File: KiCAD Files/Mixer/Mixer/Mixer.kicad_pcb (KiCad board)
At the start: 4 copper layers, 59 x 30.5 mm, 64 parts, among them IC1 FST3253MTCX, K1 G6K-2F-Y DC3, U1 OPA1678IDGKT, U2 OPA1678IDGKT, U3 OPA1678IDGKT, U4 NC7SZ04P5X, U5 4053, U6 4053

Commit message: update only
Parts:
- removed IQ_Clk: Conn_01x04_Socket, Connector_PinHeader_2.54mm:PinHeader_1x04_P2.54mm_Vertical
- added IQ_Clock_in1: Conn_01x03_Socket, Connector_JST:JST_EH_B3B-EH-A_1x03_P2.50mm_Vertical, F.Cu at (107.0, 82.9)
- added JP1: SolderJumper_3_Open, Jumper:SolderJumper-3_P1.3mm_Open_Pad1.0x1.5mm_NumberLabels, B.Cu at (119.9, 84.2)
- added JP2: SolderJumper_3_Open, Jumper:SolderJumper-3_P1.3mm_Open_Pad1.0x1.5mm_NumberLabels, B.Cu at (134.2, 84.8)
- added R5: 100R, Resistor_SMD:R_0805_2012Metric_Pad1.20x1.40mm_HandSolder, B.Cu at (126.4, 84.8)
- added R8: 100R, Resistor_SMD:R_0805_2012Metric_Pad1.20x1.40mm_HandSolder, B.Cu at (117.0, 75.1)
- added U2: SN74AC74PWR, Private:74AC74-L, B.Cu at (120.2, 71.2)
- renumbered IQ_Balance to IQ_Balance1, I_In_Tx to I_In_Tx1, I_Out_Rx to I_Out_Rx1, Q_In_Tx to Q_In_Tx1, Q_Out_Rx to Q_Out_Rx1, R8 to R10, R9 to R11, R10 to R12, R11 to R13, R12 to R14, R13 to R15, R14 to R16, R15 to R17, R16 to R18, R17 to R19, R18 to R20, R5 to R6, R6 to R7, R7 to R9, RF_In to RF_In1, RF_Out to RF_Out1, Supply to Supply1, Tx to Tx2, TxN to TxN1, U2 to U3, U3 to U4, U4 to U5, U5 to U6, U6 to U7
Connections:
- IC1 pad 14: /Clk_S0 -> /S0
- IC1 pad 2: /Clk_S1 -> /S1
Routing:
- net /S0: track 0.00 -> 21.2 mm
- net /Clk_S0: track 21.2 -> 0.00 mm
- net /S1: track 0.00 -> 15.7 mm
- net /Clk_S1: track 15.7 -> 0.00 mm

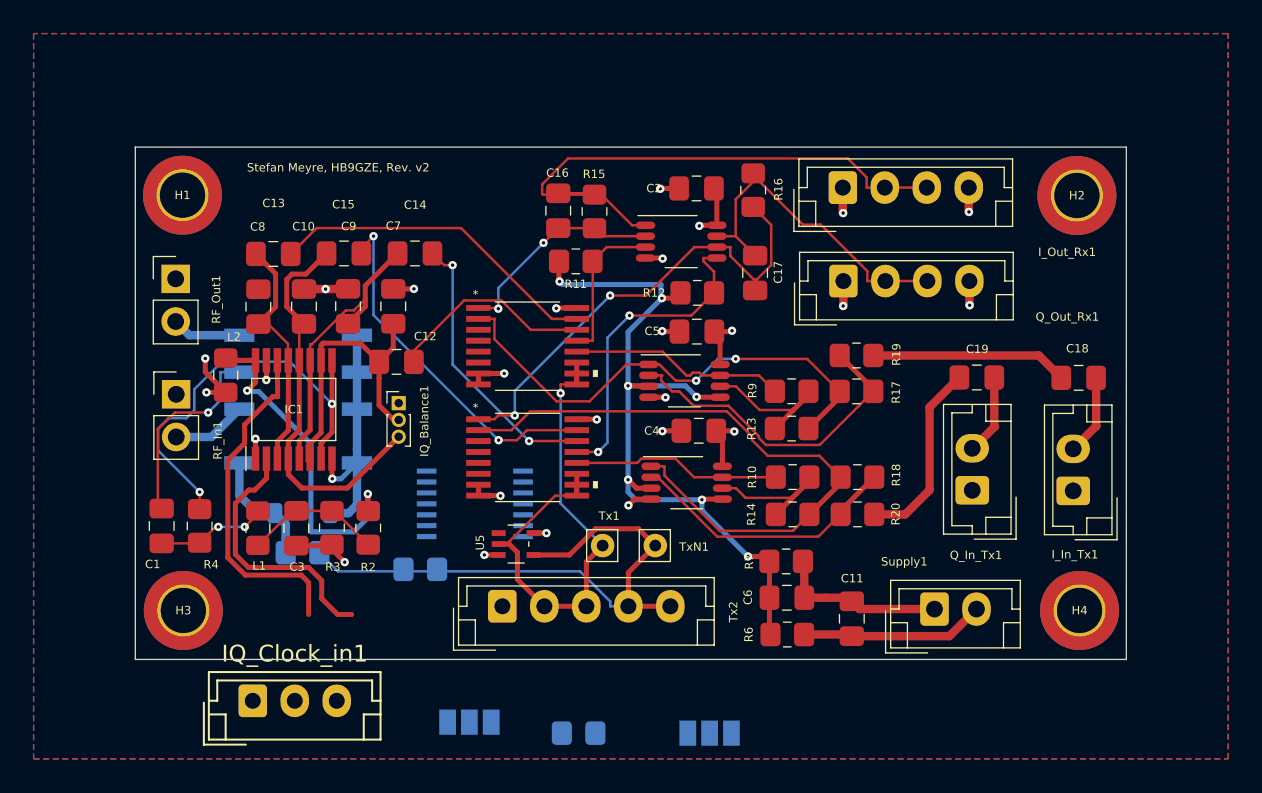
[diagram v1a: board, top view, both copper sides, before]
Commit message: added 74AC74 at mixer board
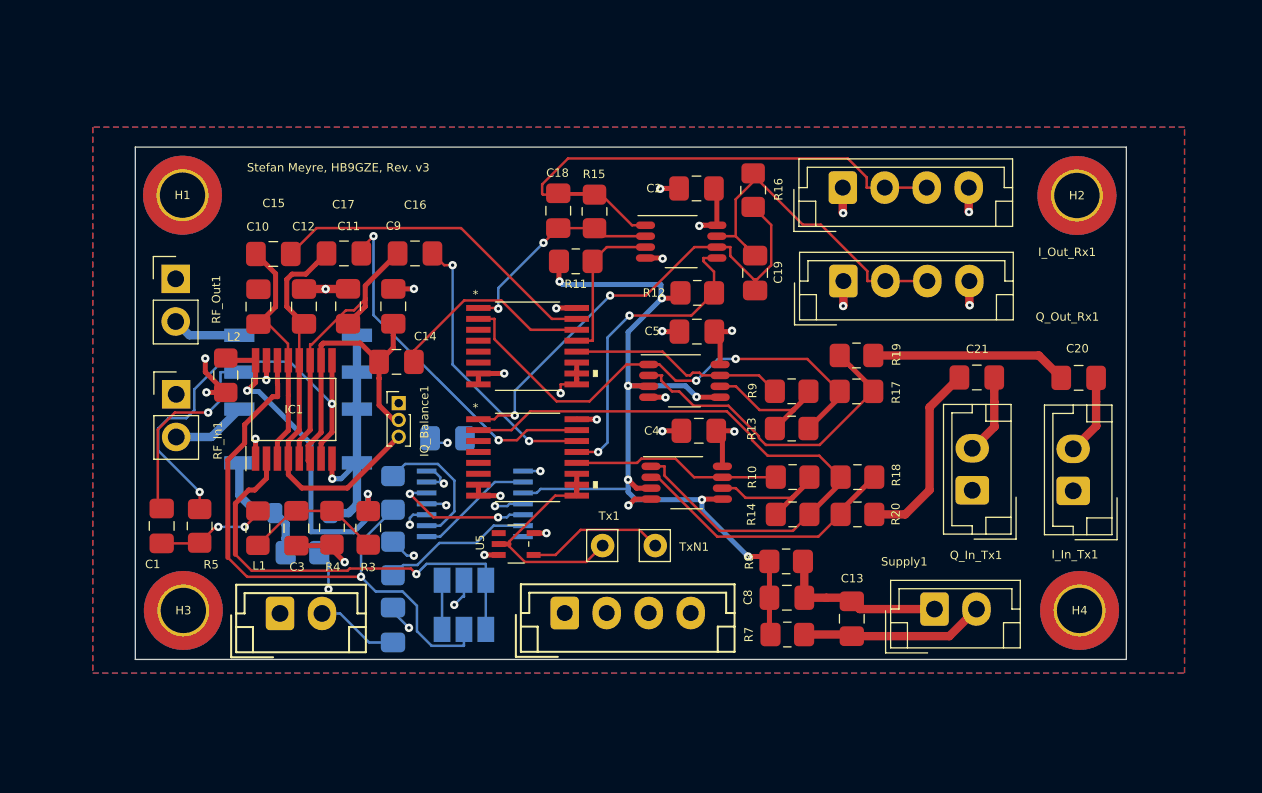
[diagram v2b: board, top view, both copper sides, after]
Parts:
- removed IQ_Clock_in1: Conn_01x03_Socket, Connector_JST:JST_EH_B3B-EH-A_1x03_P2.50mm_Vertical
- removed the R5 at (126.4, 84.8)
- removed the R8 at (117.0, 75.1)
- removed Tx2: Conn_01x05_Socket, Connector_JST:JST_EH_B5B-EH-A_1x05_P2.50mm_Vertical
- added C6: 100nF, Capacitor_SMD:C_0805_2012Metric_Pad1.18x1.45mm_HandSolder, B.Cu at (115.4, 78.4)
- added C7: 10uF, Capacitor_SMD:C_0805_2012Metric_Pad1.18x1.45mm_HandSolder, B.Cu at (118.6, 67.3)
- added J1: Conn_01x02_Socket, Connector_JST:JST_EH_B2B-EH-A_1x02_P2.50mm_Vertical, F.Cu at (108.7, 77.7)
- added J2: Conn_01x04_Socket, Connector_JST:JST_EH_B4B-EH-A_1x04_P2.50mm_Vertical, F.Cu at (125.6, 77.7)
- added R1: 100R, Resistor_SMD:R_0805_2012Metric_Pad1.20x1.40mm_HandSolder, B.Cu at (115.4, 74.4)
- added R6: 100R, Resistor_SMD:R_0805_2012Metric_Pad1.20x1.40mm_HandSolder, B.Cu at (115.4, 70.5)
- moved JP2 15.9 mm to (119.6, 78.7), turned to 0 degrees
- moved JP1 8.46 mm to (119.6, 75.7), turned to 0 degrees
- renumbered C8 to C10, C9 to C11, C10 to C12, C11 to C13, C12 to C14, C13 to C15, C14 to C16, C15 to C17, C16 to C18, C17 to C19, C18 to C20, C19 to C21, C6 to C8, C7 to C9, R1 to R2, R2 to R3, R3 to R4, R4 to R5, R6 to R7, R7 to R8
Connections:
- IC1 pad 14: /S0 -> /Clk_S0
- JP1 pad 2: Net-(JP1-C) -> /Clk_S1
- JP2 pad 2: Net-(JP2-C) -> /Clk_S0
- U2 pad 11: Net-(IQ_Clock_in1-Pin_2) -> /+2.5V
- U2 pad 3: Net-(IQ_Clock_in1-Pin_2) -> /+2.5V
- U2 pad 6: /Clk_S1 -> Net-(U2-*1Q)
- U2 pad 9: /Clk_S0 -> Net-(U2-2Q)
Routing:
- net /Clk_S0: track 0.00 -> 36.0 mm, vias 0 -> 1
- net /+2.5V: track 47.9 -> 80.0 mm, vias 7 -> 9
- net /S0: track 21.2 -> 2.93 mm
- net /S1: track 15.7 -> 26.3 mm, vias 0 -> 1
- net Net-(U2-*1Q): track 0.00 -> 8.97 mm
- net Net-(U2-1Q): track 0.00 -> 8.41 mm, vias 0 -> 2
- net +5V: track 28.6 -> 36.9 mm, vias 8 -> 13
- net Net-(U2-2Q): track 0.00 -> 8.21 mm
- net /Clk_S1: track 0.00 -> 7.27 mm, vias 0 -> 2
- net Net-(U2-*2Q): track 0.00 -> 7.09 mm
- net Net-(J1-Pin_2): track 0.00 -> 4.94 mm
- net /TxN: track 35.7 -> 38.5 mm, vias 0 -> 1
- net /Tx: track 31.9 -> 34.4 mm
- net Net-(Q_Out_Rx1-Pin_2): track 20.1 -> 21.0 mm
- net Net-(U1B-IN+): track 18.9 -> 19.5 mm
- added copper zone on In1.Cu, net +5V
- removed copper zone on In2.Cu, net +5V
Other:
- board text added: "Stefan Meyre, HB9GZE, Rev. v3"
- board text removed: "Stefan Meyre, HB9GZE, Rev. v2"

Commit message: more work on new Mixer
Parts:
- C6: footprint Capacitor_SMD:C_0805_2012Metric_Pad1.18x1.45mm_HandSolder -> Capacitor_SMD:C_0603_1608Metric_Pad1.08x0.95mm_HandSolder
- R1, R6: footprint Resistor_SMD:R_0805_2012Metric_Pad1.20x1.40mm_HandSolder -> Resistor_SMD:R_0603_1608Metric_Pad0.98x0.95mm_HandSolder
- moved R6 0.33 mm to (115.5, 70.2)
- moved R1 0.33 mm to (115.4, 74.1)
- moved C6 0.06 mm to (115.4, 78.3)
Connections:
- IC1 pad 14: /Clk_S0 -> /S0
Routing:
- net /Clk_S0: track 36.0 -> 14.8 mm, vias 1 -> 0
- net /S0: track 2.93 -> 22.5 mm, vias 0 -> 2
- net /Tx: track 34.4 -> 35.9 mm

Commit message: added ti mixer board
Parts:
- added C1: 100nF, Capacitor_SMD:C_0603_1608Metric_Pad1.08x0.95mm_HandSolder, B.Cu at (108.2, 57.9)
- added C4: 100nF, Capacitor_SMD:C_0603_1608Metric_Pad1.08x0.95mm_HandSolder, B.Cu at (105.3, 56.9)
- added C8: 1uF, Capacitor_SMD:C_0805_2012Metric_Pad1.18x1.45mm_HandSolder, B.Cu at (108.5, 52.0)
- added C9: 100nF, Capacitor_SMD:C_0603_1608Metric_Pad1.08x0.95mm_HandSolder, B.Cu at (111.5, 52.6)
- added L3: 100u, Inductor_SMD:L_0805_2012Metric_Pad1.15x1.40mm_HandSolder, B.Cu at (114.4, 52.6)
- added U1: BGA420H6327XTSA1, Private:PG-SOT343-4-1_INF, B.Cu at (108.6, 54.9)
- renumbered C8 to C10, C13 to C11, C6 to C12, C9 to C13, C10 to C14, C11 to C15, C12 to C16, C7 to C17, C14 to C18, C15 to C19, C16 to C20, C17 to C21, C18 to C22, C19 to C23, C20 to C24, C21 to C25, C1 to C3, C3 to C5, C4 to C6, C5 to C7, J1 to Clock_In, I_In_Tx1 to I_In_Tx, I_Out_Rx1 to I_Out_Rx, J2 to J1, Q_In_Tx1 to Q_In_Tx, Q_Out_Rx1 to Q_Out_Rx, R2 to R1, R3 to R2, R4 to R3, R5 to R4, R1 to R5, R7 to R6, R8 to R7, R6 to R8, RF_In1 to RF_In, RF_Out1 to RF_Out, Supply1 to Supply, Tx1 to Tx, TxN1 to TxN, U1 to U2, U2 to U5, U5 to U8
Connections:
- K1 pad 4: /RF_Out -> Net-(C1-Pad1)
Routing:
- net Net-(U1-VD): track 0.00 -> 6.28 mm
- net Net-(C1-Pad1): track 0.00 -> 4.42 mm
- net Net-(U1-OUT): track 0.00 -> 3.54 mm
- net Net-(U1-IN): track 0.00 -> 2.00 mm
- net +5V: track 36.9 -> 38.3 mm, vias 13 -> 14
- added copper zone on In2.Cu, net +5V
- removed copper zone on In1.Cu, net GND
